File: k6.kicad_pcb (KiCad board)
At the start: 2 copper layers, 41 parts, among them J1 USB_C_Receptacle_USB2.0, J2 Conn_02x05_Odd_Even, SW1 SW_SPDT, SW2 SW_Push, U1 STM32F042K6T6, U2 MCP1700-3302E_SOT23

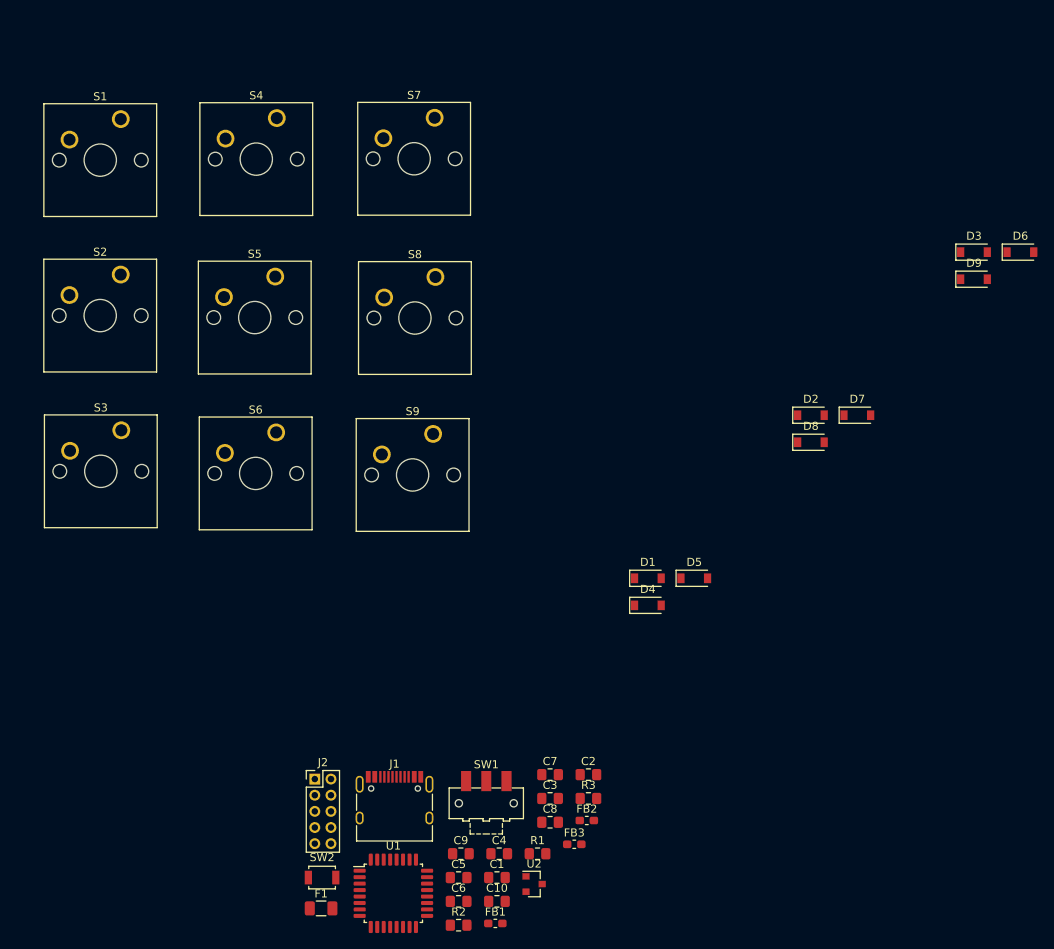
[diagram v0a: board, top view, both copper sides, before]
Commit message: Move parts - part one
No traces yet, only part movement
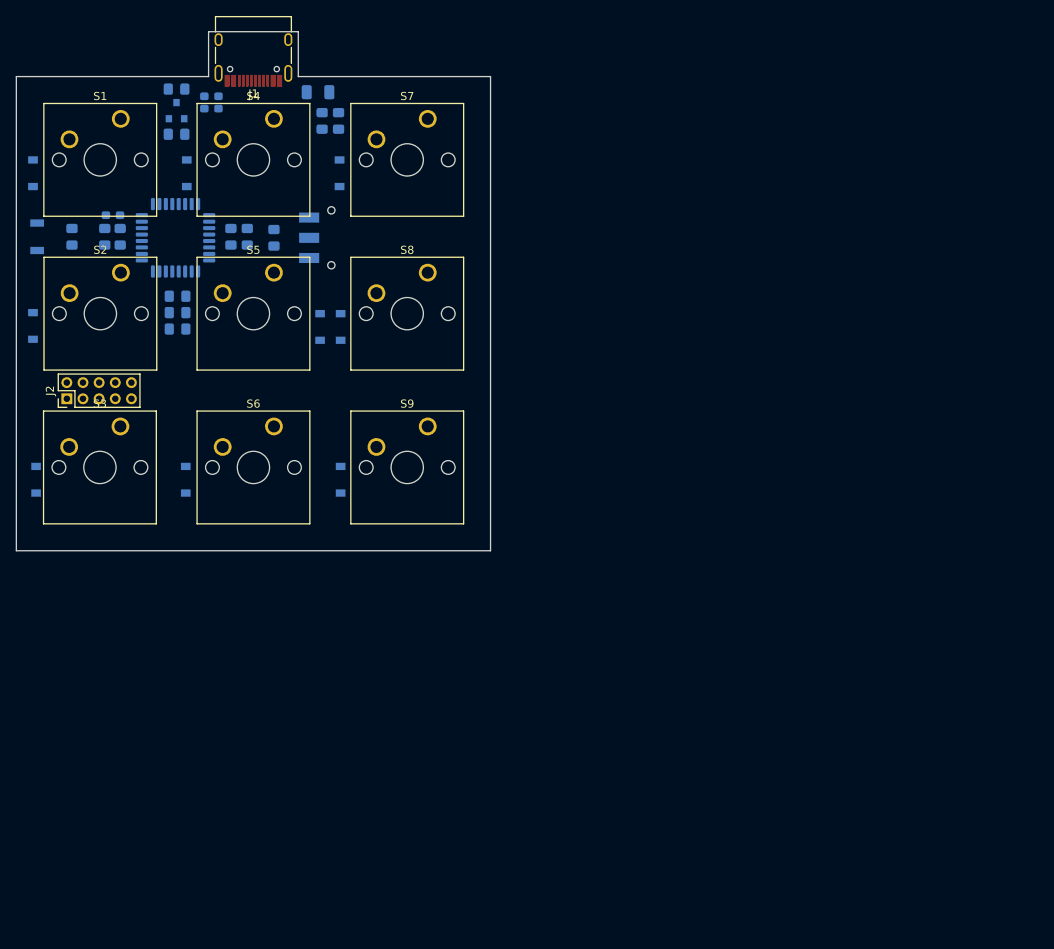
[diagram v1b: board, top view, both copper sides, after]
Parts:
- C1, C10, C2, C3, C4, C5, C6, C7, C8, C9, D1, D2, D3, D4, D5, D6, D7, D8, D9, F1, FB1, FB2, FB3, R1, R2, R3, SW1, SW2, U1, U2: moved to B.Cu
- moved D3 119.5 mm to (27.1, 74.5), turned to 90 degrees
- moved FB1 108.3 mm to (48.8, 27.1), turned to 180 degrees
- moved D6 107.2 mm to (45.6, 74.5), turned to 90 degrees
- moved U2 105.5 mm to (44.5, 28.8), turned to 90 degrees
- moved F1 101.1 mm to (62.0, 26.5), turned to 180 degrees
- moved R2 101.0 mm to (62.5, 30.1), turned to 90 degrees
- moved FB2 99.7 mm to (48.8, 28.6)
- moved C2 99.1 mm to (44.5, 26.2)
- moved D2 97.0 mm to (26.7, 55.5), turned to 90 degrees
- moved FB3 96.6 mm to (36.6, 41.8)
- moved J1 95.9 mm to (54.0, 21.1), turned to 180 degrees
- moved C1 95.2 mm to (31.5, 44.5), turned to 270 degrees
- moved C3 94.4 mm to (44.5, 31.8)
- moved C6 93.3 mm to (35.6, 44.5), turned to 270 degrees
- moved D1 91.2 mm to (26.7, 36.6), turned to 90 degrees
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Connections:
- J1 pad A8: Net-(J1-PadA8) -> (no net)
- J1 pad B8: Net-(J1-PadB8) -> (no net)
- J2 pad 6: Net-(J2-Pad6) -> (no net)
- J2 pad 7: Net-(J2-Pad7) -> (no net)
- J2 pad 8: Net-(J2-Pad8) -> (no net)
- S1 pad 1: (no net) -> COL0
- S1 pad 2: (no net) -> Net-(D1-Pad2)
- S2 pad 1: (no net) -> COL0
- S2 pad 2: (no net) -> Net-(D2-Pad2)
- S3 pad 1: (no net) -> COL0
- S3 pad 2: (no net) -> Net-(D3-Pad2)
- S4 pad 1: (no net) -> COL1
- S4 pad 2: (no net) -> Net-(D4-Pad2)
- S5 pad 1: (no net) -> COL1
- S5 pad 2: (no net) -> Net-(D5-Pad2)
- S6 pad 1: (no net) -> COL1
- S6 pad 2: (no net) -> Net-(D6-Pad2)
- S7 pad 1: (no net) -> COL2
- S7 pad 2: (no net) -> Net-(D7-Pad2)
- S8 pad 1: (no net) -> COL2
- S8 pad 2: (no net) -> Net-(D8-Pad2)
- S9 pad 1: (no net) -> COL2
- S9 pad 2: (no net) -> Net-(D9-Pad2)
- U1 pad 12: Net-(U1-Pad12) -> (no net)
- U1 pad 13: Net-(U1-Pad13) -> (no net)
- U1 pad 14: Net-(U1-Pad14) -> (no net)
- U1 pad 15: Net-(U1-Pad15) -> (no net)
- U1 pad 18: Net-(U1-Pad18) -> (no net)
- U1 pad 19: Net-(U1-Pad19) -> (no net)
- U1 pad 2: Net-(U1-Pad2) -> (no net)
- U1 pad 20: Net-(U1-Pad20) -> (no net)
- U1 pad 25: Net-(U1-Pad25) -> (no net)
- U1 pad 26: Net-(U1-Pad26) -> (no net)
- U1 pad 27: Net-(U1-Pad27) -> (no net)
- U1 pad 28: Net-(U1-Pad28) -> (no net)
- U1 pad 29: Net-(U1-Pad29) -> (no net)
- U1 pad 3: Net-(U1-Pad3) -> (no net)
- U1 pad 30: Net-(U1-Pad30) -> (no net)
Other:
- board outline added: 58.7 x 64.3 mm

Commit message: Add some tracks - hate it
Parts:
- moved J2 36.7 mm to (64.5, 49.9), turned to 180 degrees
- moved SW1 29.4 mm to (44.3, 66.8), turned to 180 degrees
- moved R1 19.8 mm to (44.3, 60.2), turned to 270 degrees
- moved C7 0.18 mm to (44.5, 54.0)
- moved C10 0.18 mm to (44.5, 51.9)
- moved C4 0.18 mm to (44.5, 56.0)
- turned C5 to 90 degrees
- turned C8 to 90 degrees
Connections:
- J1 pad A8: (no net) -> Net-(J1-PadA8)
- J1 pad B8: (no net) -> Net-(J1-PadB8)
- J2 pad 6: (no net) -> Net-(J2-Pad6)
- J2 pad 7: (no net) -> Net-(J2-Pad7)
- J2 pad 8: (no net) -> Net-(J2-Pad8)
- U1 pad 12: (no net) -> ROW0
- U1 pad 13: (no net) -> ROW1
- U1 pad 14: (no net) -> Net-(U1-Pad14)
- U1 pad 15: (no net) -> Net-(U1-Pad15)
- U1 pad 18: (no net) -> ROW2
- U1 pad 19: (no net) -> Net-(U1-Pad19)
- U1 pad 2: (no net) -> Net-(U1-Pad2)
- U1 pad 20: (no net) -> Net-(U1-Pad20)
- U1 pad 25: (no net) -> Net-(U1-Pad25)
- U1 pad 26: (no net) -> Net-(U1-Pad26)
- U1 pad 27: (no net) -> Net-(U1-Pad27)
- U1 pad 28: (no net) -> Net-(U1-Pad28)
- U1 pad 29: (no net) -> Net-(U1-Pad29)
- U1 pad 3: (no net) -> Net-(U1-Pad3)
- U1 pad 30: (no net) -> Net-(U1-Pad30)
- U1 pad 6: ROW0 -> Net-(U1-Pad6)
- U1 pad 7: ROW1 -> Net-(U1-Pad7)
- U1 pad 8: ROW2 -> Net-(U1-Pad8)
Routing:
- net GND: track 0.00 -> 40.2 mm, vias 0 -> 2
- net ROW1: track 0.00 -> 38.2 mm
- net COL2: track 0.00 -> 38.1 mm
- net COL1: track 0.00 -> 38.1 mm
- net ROW0: track 0.00 -> 38.0 mm
- net ROW2: track 0.00 -> 37.7 mm
- net +3V3: track 0.00 -> 27.3 mm, vias 0 -> 2
- net NRST: track 0.00 -> 18.2 mm, vias 0 -> 2
- net SWDIO: track 0.00 -> 15.7 mm
- net SWDCLK: track 0.00 -> 14.3 mm, vias 0 -> 2
- net Net-(D5-Pad2): track 0.00 -> 13.1 mm
- net Net-(R1-Pad1): track 0.00 -> 11.3 mm, vias 0 -> 2
- net +3.3VA: track 0.00 -> 6.60 mm
- net Net-(D4-Pad2): track 0.00 -> 5.10 mm
- net Net-(D3-Pad2): track 0.00 -> 5.10 mm
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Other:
- net class Default: trace_width 0.25 -> 0.254
- net class Power added: clearance 0.2, trace_width 0.381, via_dia 0.8, via_drill 0.4
